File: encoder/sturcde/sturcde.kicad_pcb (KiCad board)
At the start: 2 copper layers, 61 x 69.8 mm, 14 parts, among them J1 Left A, J2 Left B, J3 Left Encoder, J4 Right A, J5 Right B, J6 Right Encoder

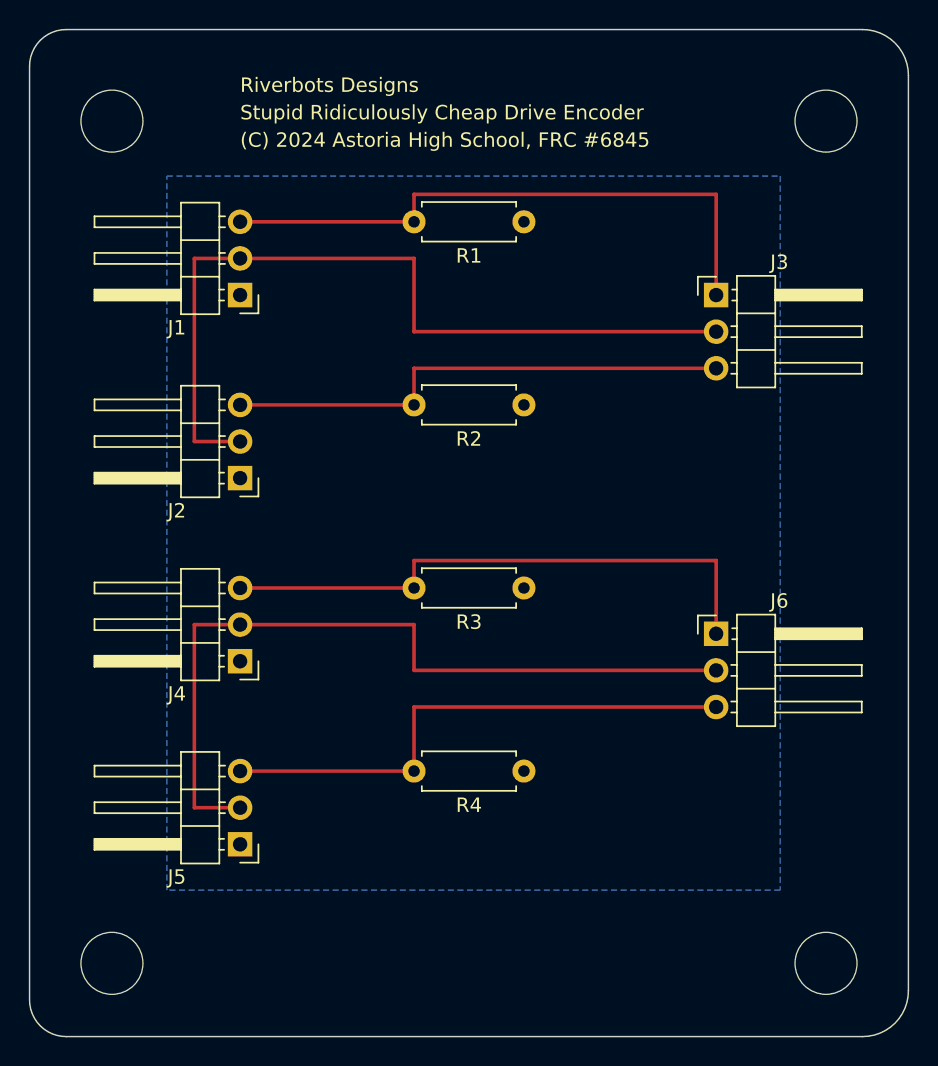
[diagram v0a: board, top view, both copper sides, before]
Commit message: Add logo; general cleanups and prep for pcbway.
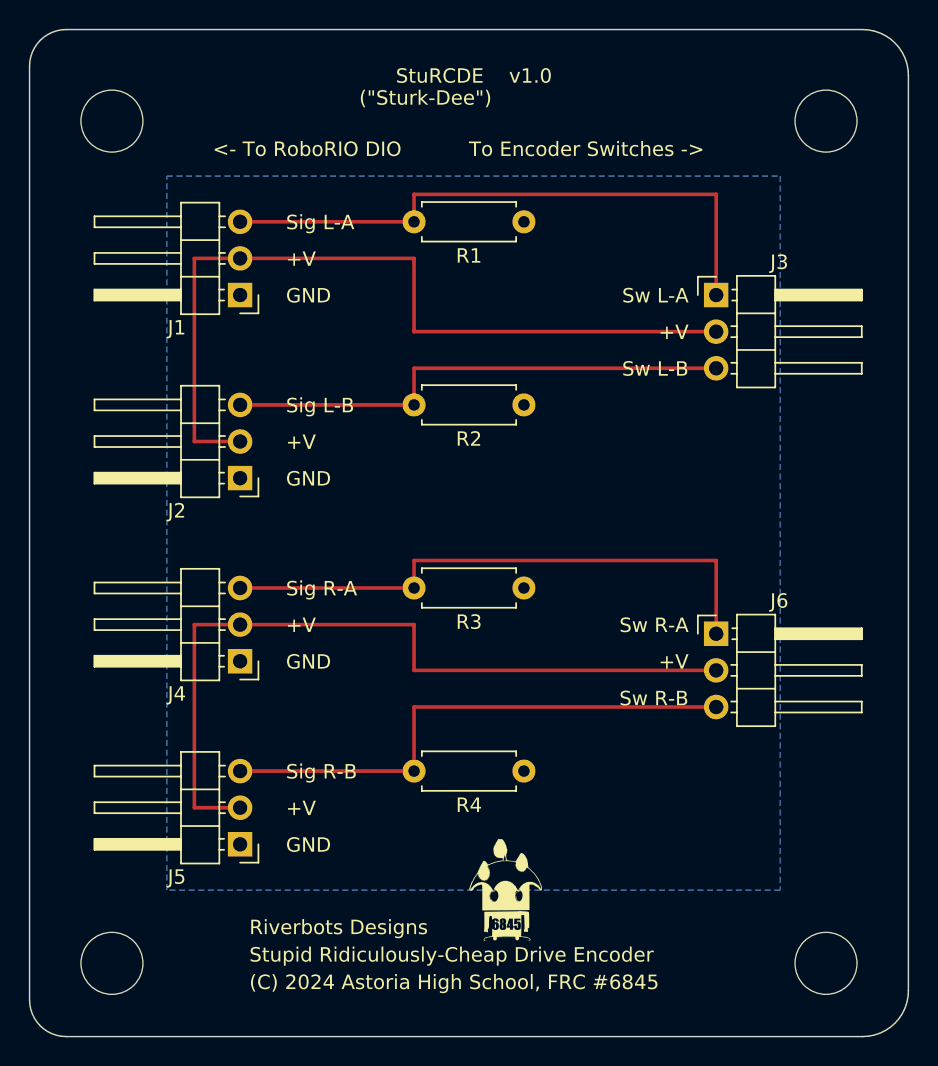
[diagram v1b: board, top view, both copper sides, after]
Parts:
- added G***: LOGO, Library:Riverbots 6845 Logo, F.Cu at (94.0, 91.4)
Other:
- board text added: "({dblquote}Sturk-Dee{dblquote})"
- board text added: "+V"
- board text added: "<- To RoboRIO DIO"
- board text added: "GND"
- board text added: "Sig L-A"
- board text added: "Sig L-B"
- board text added: "Sig R-A"
- board text added: "Sig R-B"
- board text added: "StuRCDE v1.0"
- board text added: "Stupid Ridiculously-Cheap Drive Encoder"
- board text added: "Sw L-A"
- board text added: "Sw L-B"
- board text added: "Sw R-A"
- board text added: "Sw R-B"
- board text added: "To Encoder Switches ->"
- board text removed: "Stupid Ridiculously Cheap Drive Encoder"
